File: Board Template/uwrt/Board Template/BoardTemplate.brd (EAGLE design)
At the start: 101.7 x 101.6 mm, 18 parts, among them P1 39-30-06?, P2 39-30-06?, P3 39-30-06?, P4 39-30-08?, P5 39-30-08?, P6 39-30-02?

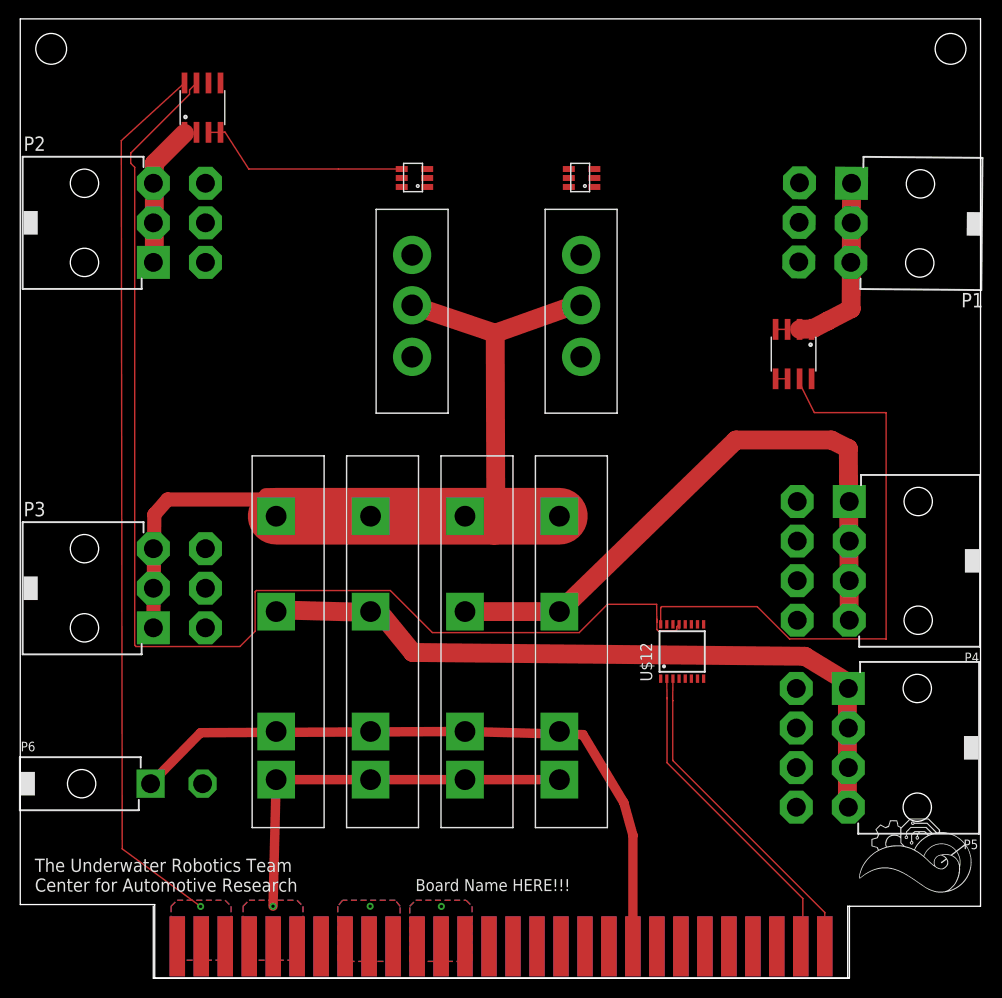
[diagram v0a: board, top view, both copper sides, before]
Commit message: Changed Battery Balancer
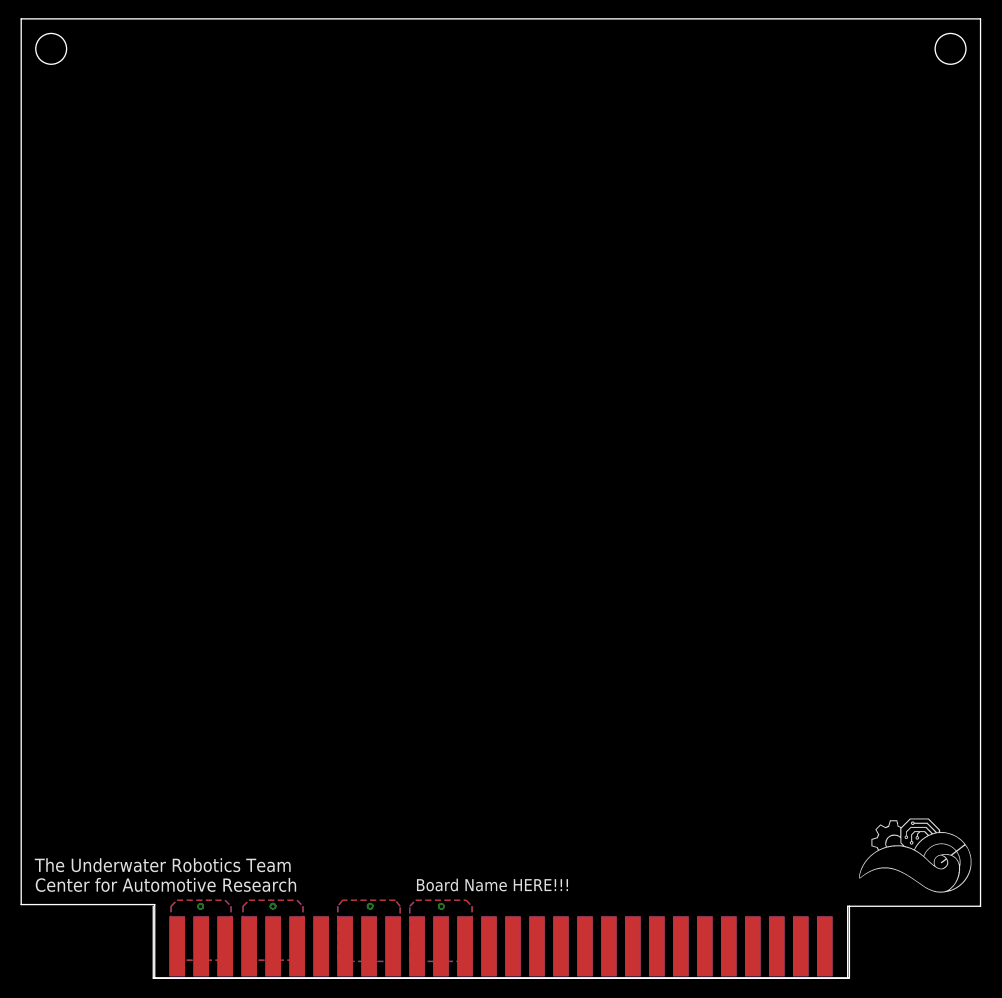
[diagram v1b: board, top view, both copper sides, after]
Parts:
- removed P1, P2, P3: 39-30-06?, con-molex-mini-fit:39-30-?06?
- removed P4, P5: 39-30-08?, con-molex-mini-fit:39-30-?08?
- removed P6: 39-30-02?, con-molex-mini-fit:39-30-?02?
- removed U$10, U$11, U$8, U$9: CMX60D20, CMX60D20:CMX60D20
- removed U$12: ADC128D818, ADC128D818:TSSOP-16
- removed U$2, U$3: LM5050, LM5050:LM5050
- removed U$4, U$5: IXFX64N60P3, IXFX64N60P3:IXFX64N60P3
- removed U$6, U$7: ACS722, ACS722:SOIC-8
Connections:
- removed net BALANCED_OUT: P3.1, P3.2, P3.3, U$2.1, U$2.6, U$3.1, U$3.6, U$4.DRAIN, U$5.DRAIN
- removed net KILL_SWITCH: P6.1, U$1.37, U$10.CONTROL+, U$11.CONTROL+, U$8.CONTROL+, U$9.CONTROL+
- removed net LOAD: U$10.LOAD+, U$11.LOAD+, U$8.LOAD+, U$9.LOAD+
- removed net MOTOR_POWER1: P5.1, P5.2, P5.3, P5.4, U$8.LOAD-, U$9.LOAD-
- removed net MOTOR_POWER2: P4.1, P4.2, P4.3, P4.4, U$10.LOAD-, U$11.LOAD-
- removed net N$1: U$2.4, U$4.SOURCE, U$6.IP-1, U$6.IP-2
- removed net N$2: U$2.5, U$4.GATE
- removed net N$4: U$3.4, U$5.SOURCE, U$7.IP-1, U$7.IP-2
- removed net N$5: U$3.5, U$5.GATE
- removed net PORT_BATTERY: P1.1, P1.2, P1.3, U$6.IP+1, U$6.IP+2
- removed net PORT_CURRENT: U$12.IN0, U$6.VIOUT
- removed net SENSOR_SCL: U$1.29, U$12.SCL
- removed net SENSOR_SDA: U$1.30, U$12.SDA
- removed net STBD_BATTERY: P2.1, P2.2, P2.3, U$7.IP+1, U$7.IP+2
- removed net STBD_CURRENT: U$12.IN3, U$7.VIOUT
- net +3V3: no longer U$6.VCC, U$7.VCC
- net GND: no longer P1.4, P1.5, P1.6, P2.4, P2.5, P2.6, P3.4, P3.5, P3.6, P4.5, P4.6, P4.7, P4.8, P5.5, P5.6, P5.7, P5.8, U$10.CONTROL-, U$11.CONTROL-, U$2.2, U$3.2, U$6.BW_SEL, U$6.GND, U$7.BW_SEL, U$7.GND, U$8.CONTROL-, U$9.CONTROL-
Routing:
- net STBD_CURRENT: track 132.3 -> 0.00 mm
- net +3V3: track 94.4 -> 0.00 mm
- net BALANCED_OUT: track 85.6 -> 0.00 mm
- net MOTOR_POWER1: track 76.2 -> 0.00 mm
- net KILL_SWITCH: track 71.8 -> 0.00 mm
- net MOTOR_POWER2: track 66.4 -> 0.00 mm
- net PORT_CURRENT: track 62.8 -> 0.00 mm
- net GND: track 44.7 -> 0.00 mm
- net SENSOR_SCL: track 35.0 -> 0.00 mm
- net SENSOR_SDA: track 34.5 -> 0.00 mm
- net LOAD: track 30.0 -> 0.00 mm
- net N$4: track 22.6 -> 0.00 mm
- net PORT_BATTERY: track 21.2 -> 0.00 mm
- net STBD_BATTERY: track 15.1 -> 0.00 mm
- net N$1: track 1.27 -> 0.00 mm
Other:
- board size 101.7 x 101.6 mm -> 101.6 x 101.6 mm
